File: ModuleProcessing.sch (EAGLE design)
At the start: 24 parts, among them IC1 INA128U, IC2 LM358MX, IC3 MCP606-I_SN

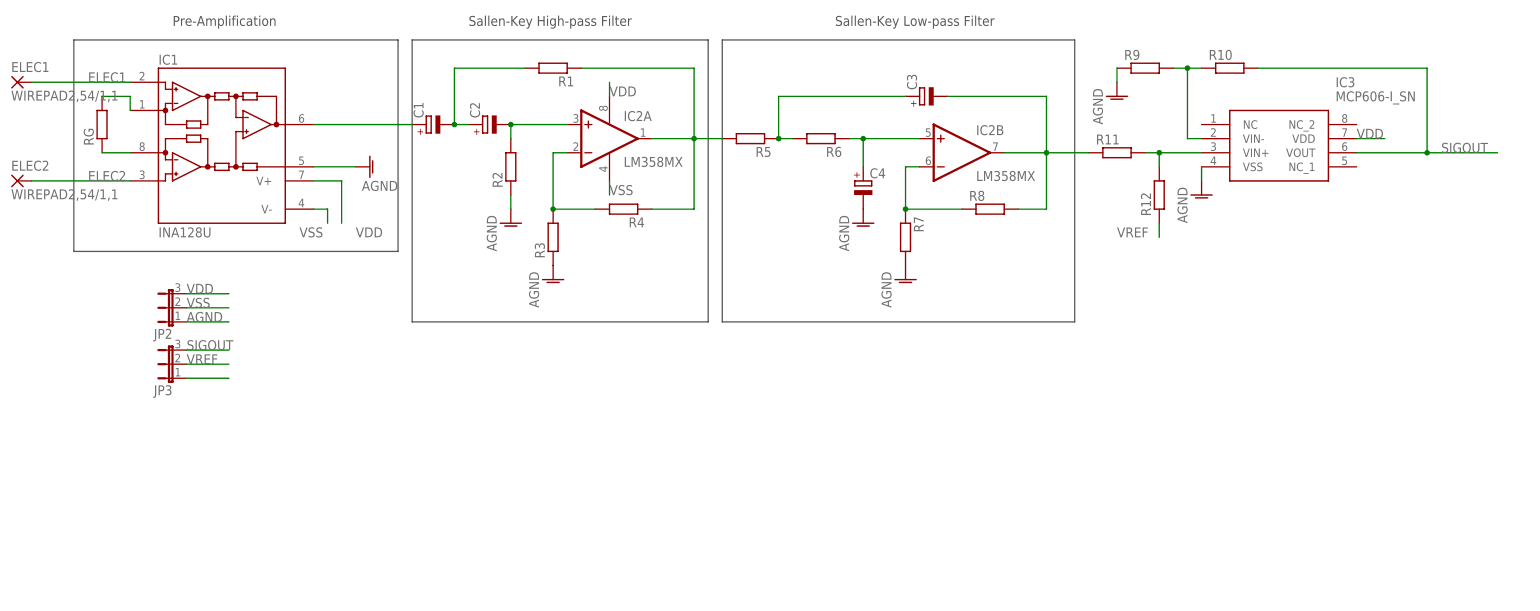
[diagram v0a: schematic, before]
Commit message: Added bypass capacitors on Processing Module
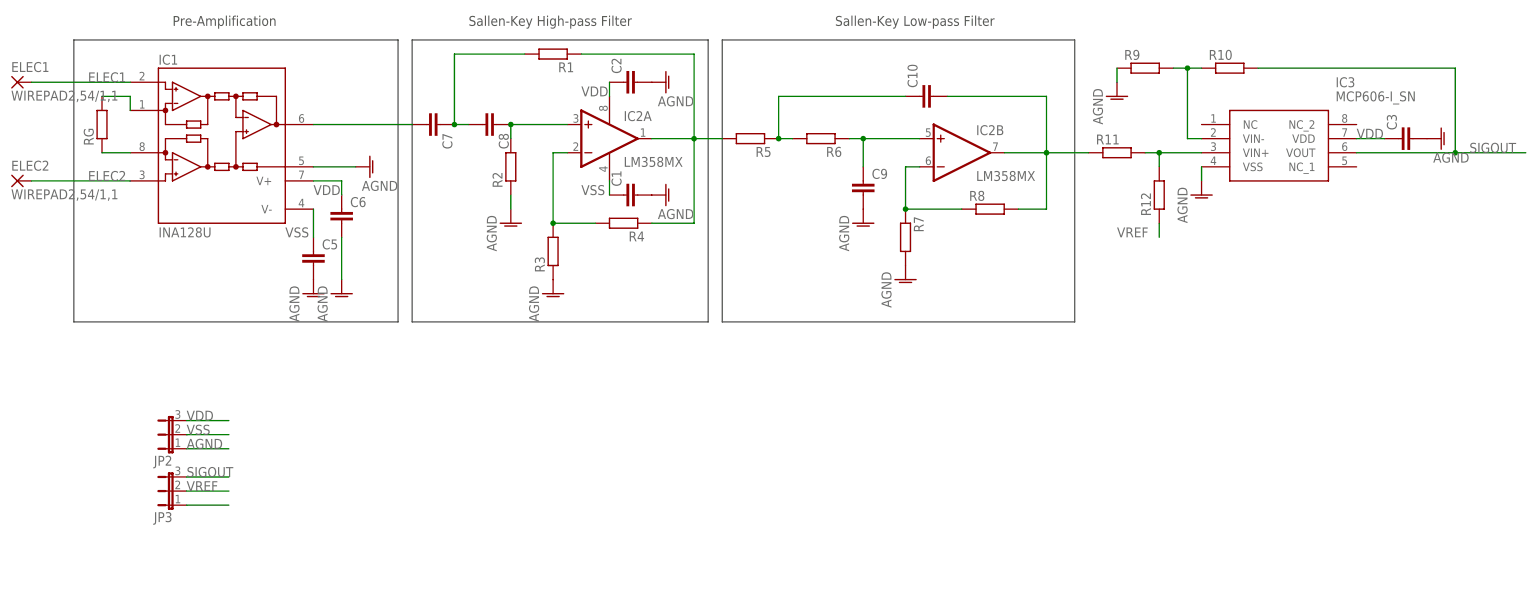
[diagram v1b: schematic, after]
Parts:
- removed C4: (no value), rcl:CPOL-EUE3.5-8
- added C10, C5, C6, C7, C8, C9: (no value), rcl:C-EUC0603
- C1, C2, C3: device rcl:CPOL-EUE3.5-8 -> rcl:C-EUC0603
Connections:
- net AGND: now also C1.2, C2.2, C3.2, C5.2, C6.2, C9.2; no longer C4.-
- net N$10: now also C10.2; no longer C3.-
- net N$5: now also C8.1; no longer C2.-
- net N$6: now also C7.1, C8.2; no longer C1.-, C2.+
- net N$7: now also C7.2; no longer C1.+
- net N$8: now also C10.1; no longer C3.+
- net N$9: now also C9.1; no longer C4.+
- net VDD: now also C2.1, C3.1, C6.1
- net VSS: now also C1.1, C5.1
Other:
- moved on the sheet: JP2, JP3, R1, R3, R4

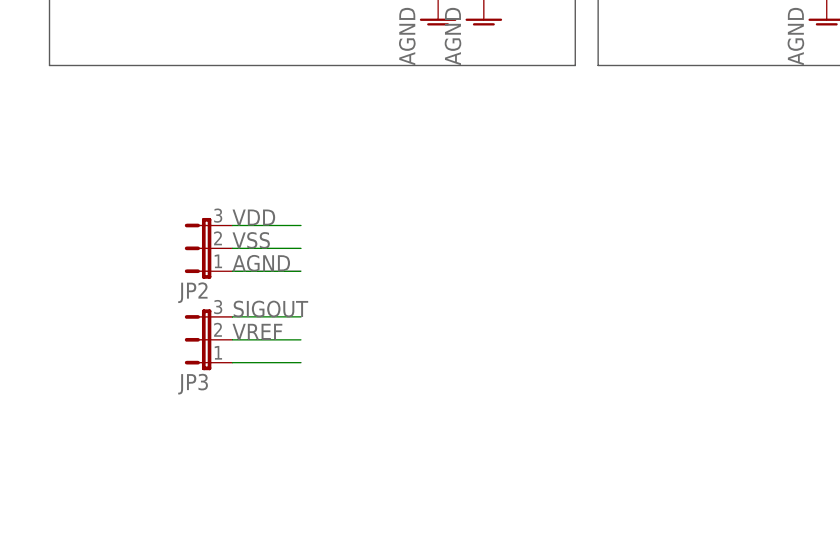
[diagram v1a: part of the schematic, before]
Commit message: Changed board for testing before final prototype
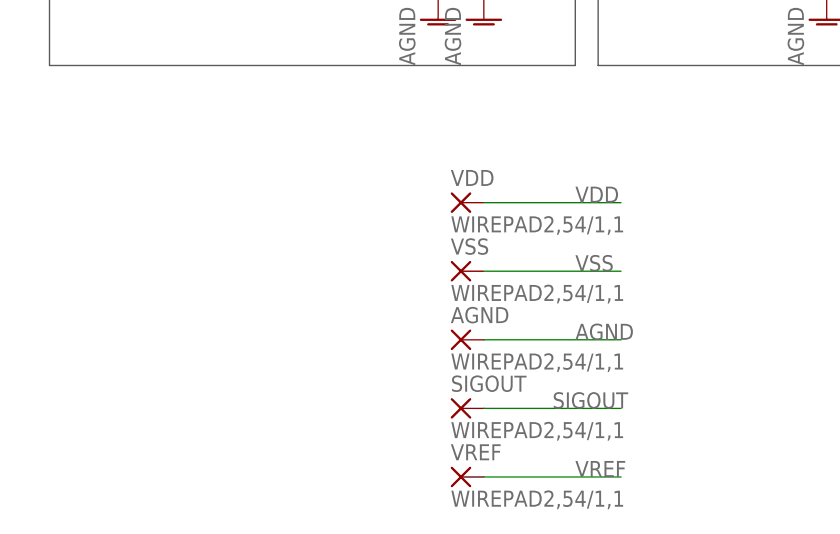
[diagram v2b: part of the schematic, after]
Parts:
- removed JP2, JP3: (no value), jumper:JP2E
- added AGND, SIGOUT, VDD, VREF, VSS: WIREPAD2,54/1,1, wirepad:WIREPAD2,54/1,1
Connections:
- removed net N$19: JP3.1
- net AGND: now also AGND.P; no longer JP2.1
- net SIGOUT: now also SIGOUT.P; no longer JP3.3
- net VDD: now also VDD.P; no longer JP2.3
- net VREF: now also VREF.P; no longer JP3.2
- net VSS: now also VSS.P; no longer JP2.2
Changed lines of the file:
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@@
 </variantdefs>
 <classes>
-<class number="0" name="default" width="0.254" drill="0.3048">
+<class number="0" name="default" width="0.4064" drill="0.5588">
 <clearance class="0" value="0.254"/>
 </class>
@@
 <part name="ELEC1" library="wirepad" library_urn="urn:adsk.eagle:library:412" deviceset="WIREPAD" device="2,54/1,1" package3d_urn="urn:adsk.eagle:package:30836/1"/>
 <part name="ELEC2" library="wirepad" library_urn="urn:adsk.eagle:library:412" deviceset="WIREPAD" device="2,54/1,1" package3d_urn="urn:adsk.eagle:package:30836/1"/>
-<part name="JP2" library="jumper" library_urn="urn:adsk.eagle:library:252" deviceset="JP2E" device="" package3d_urn="urn:adsk.eagle:package:15452/1"/>
-<part name="JP3" library="jumper" library_urn="urn:adsk.eagle:library:252" deviceset="JP2E" device="" package3d_urn="urn:adsk.eagle:package:15452/1"/>
 <part name="C5" library="rcl" library_urn="urn:adsk.eagle:library:334" deviceset="C-EU" device="C0603" package3d_urn="urn:adsk.eagle:package:23616/2"/>
 <part name="C6" library="rcl" library_urn="urn:adsk.eagle:library:334" deviceset="C-EU" device="C0603" package3d_urn="urn:adsk.eagle:package:23616/2"/>
@@
 <part name="C3" library="rcl" library_urn="urn:adsk.eagle:library:334" deviceset="C-EU" device="C0603" package3d_urn="urn:adsk.eagle:package:23616/2"/>
 <part name="AGND12" library="supply1" library_urn="urn:adsk.eagle:library:371" deviceset="AGND" device=""/>
+<part name="VDD" library="wirepad" library_urn="urn:adsk.eagle:library:412" deviceset="WIREPAD" device="2,54/1,1" package3d_urn="urn:adsk.eagle:package:30836/1"/>
+<part name="VSS" library="wirepad" library_urn="urn:adsk.eagle:library:412" deviceset="WIREPAD" device="2,54/1,1" package3d_urn="urn:adsk.eagle:package:30836/1"/>
+<part name="AGND" library="wirepad" library_urn="urn:adsk.eagle:library:412" deviceset="WIREPAD" device="2,54/1,1" package3d_urn="urn:adsk.eagle:package:30836/1"/>
+<part name="SIGOUT" library="wirepad" library_urn="urn:adsk.eagle:library:412" deviceset="WIREPAD" device="2,54/1,1" package3d_urn="urn:adsk.eagle:package:30836/1"/>
+<part name="VREF" library="wirepad" library_urn="urn:adsk.eagle:library:412" deviceset="WIREPAD" device="2,54/1,1" package3d_urn="urn:adsk.eagle:package:30836/1"/>
 </parts>
 <sheets>
@@
 <instance part="ELEC1" gate="G$1" x="12.7" y="66.04"/>
 <instance part="ELEC2" gate="G$1" x="12.7" y="48.26"/>
-<instance part="JP2" gate="1" x="40.64" y="2.54" rot="R90"/>
-<instance part="JP3" gate="1" x="40.64" y="-7.62" rot="R90"/>
 <instance part="C5" gate="G$1" x="66.04" y="35.56"/>
 <instance part="C6" gate="G$1" x="71.12" y="43.18"/>
@@
 <instance part="C3" gate="G$1" x="261.62" y="55.88" rot="R90"/>
 <instance part="AGND12" gate="VR1" x="269.24" y="55.88" rot="R90"/>
+<instance part="VDD" gate="G$1" x="68.58" y="7.62"/>
+<instance part="VSS" gate="G$1" x="68.58" y="0"/>
+<instance part="AGND" gate="G$1" x="68.58" y="-7.62"/>
+<instance part="SIGOUT" gate="G$1" x="68.58" y="-15.24"/>
+<instance part="VREF" gate="G$1" x="68.58" y="-22.86"/>
 </instances>
 <busses>
@@
 </segment>
 <segment>
-<pinref part="JP2" gate="1" pin="1"/>
-<wire x1="43.18" y1="0" x2="50.8" y2="0" width="0.1524" layer="91"/>
-<label x="43.18" y="0" size="1.778" layer="95"/>
-</segment>
-<segment>
 <pinref part="C5" gate="G$1" pin="2"/>
 <pinref part="AGND8" gate="VR1" pin="AGND"/>
@@
 <pinref part="C3" gate="G$1" pin="2"/>
 <pinref part="AGND12" gate="VR1" pin="AGND"/>
+</segment>
+<segment>
+<pinref part="AGND" gate="G$1" pin="P"/>
+<wire x1="71.12" y1="-7.62" x2="86.36" y2="-7.62" width="0.1524" layer="91"/>
+<label x="81.28" y="-7.62" size="1.778" layer="95"/>
 </segment>
 </net>
@@
 </segment>
 <segment>
-<pinref part="JP3" gate="1" pin="3"/>
-<wire x1="43.18" y1="-5.08" x2="50.8" y2="-5.08" width="0.1524" layer="91"/>
-<label x="43.18" y="-5.08" size="1.778" layer="95"/>
+<pinref part="SIGOUT" gate="G$1" pin="P"/>
+<wire x1="71.12" y1="-15.24" x2="86.36" y2="-15.24" width="0.1524" layer="91"/>
+<label x="78.74" y="-15.24" size="1.778" layer="95"/>
 </segment>
 </net>
@@
 <label x="114.3" y="63.5" size="1.778" layer="95"/>
 <pinref part="C2" gate="G$1" pin="1"/>
-</segment>
-<segment>
-<pinref part="JP2" gate="1" pin="3"/>
-<wire x1="43.18" y1="5.08" x2="50.8" y2="5.08" width="0.1524" layer="91"/>
-<label x="43.18" y="5.08" size="1.778" layer="95"/>
 </segment>
 <segment>
@@
 <label x="66.04" y="45.72" size="1.778" layer="95"/>
 </segment>
+<segment>
+<pinref part="VDD" gate="G$1" pin="P"/>
+<wire x1="71.12" y1="7.62" x2="86.36" y2="7.62" width="0.1524" layer="91"/>
+<label x="81.28" y="7.62" size="1.778" layer="95"/>
+</segment>
 </net>
 <net name="VSS" class="0">
@@
 </segment>
 <segment>
-<pinref part="JP2" gate="1" pin="2"/>
-<wire x1="43.18" y1="2.54" x2="50.8" y2="2.54" width="0.1524" layer="91"/>
-<label x="43.18" y="2.54" size="1.778" layer="95"/>
-</segment>
-<segment>
 <pinref part="IC1" gate="G$1" pin="V-"/>
 <pinref part="C5" gate="G$1" pin="1"/>
@@
 <label x="60.96" y="38.1" size="1.778" layer="95"/>
 </segment>
+<segment>
+<pinref part="VSS" gate="G$1" pin="P"/>
+<wire x1="71.12" y1="0" x2="86.36" y2="0" width="0.1524" layer="91"/>
+<label x="81.28" y="0" size="1.778" layer="95"/>
+</segment>
 </net>
 <net name="VREF" class="0">
-<segment>
-<pinref part="JP3" gate="1" pin="2"/>
-<wire x1="43.18" y1="-7.62" x2="50.8" y2="-7.62" width="0.1524" layer="91"/>
-<label x="43.18" y="-7.62" size="1.778" layer="95"/>
-</segment>
 <segment>
 <pinref part="R12" gate="G$1" pin="1"/>
@@
 <label x="210.82" y="38.1" size="1.778" layer="95"/>
 </segment>
-</net>
-<net name="N$19" class="0">
-<segment>
-<pinref part="JP3" gate="1" pin="1"/>
-<wire x1="43.18" y1="-10.16" x2="50.8" y2="-10.16" width="0.1524" layer="91"/>
-</segment>
-</net>
+<segment>
+<pinref part="VREF" gate="G$1" pin="P"/>
+<wire x1="71.12" y1="-22.86" x2="86.36" y2="-22.86" width="0.1524" layer="91"/>
+<label x="81.28" y="-22.86" size="1.778" layer="95"/>
+</segment>
+</net>

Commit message: Final version of processing pre-prototype
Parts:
- removed C10: (no value), rcl:C-EUC0603
- removed R1: (no value), rcl:R-EU_0207/10
- added C4: (no value), rcl:C-EUC0603
- added R13: (no value), rcl:R-EU_0207/10
- renumbered AGND to PAD5, ELEC1 to PAD1, ELEC2 to PAD2, SIGOUT to PAD6, VDD to PAD3, VREF to PAD7, VSS to PAD4
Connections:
- net AGND: now also C7.2, R11.1, R4.1, R8.2; no longer C3.2, R3.1, R7.2, R9.1
- net N$10: now also C8.2, R10.1, R9.2; no longer C10.2, R11.1, R8.2
- net N$11: now also R9.1; no longer R7.1
- net N$12: now also R10.2; no longer R11.2
- net N$13: now also R11.2, R13.1; no longer R10.1, R9.2
- net N$3: now also R5.2; no longer R3.2
- net N$4: now also R3.1, R5.1, R6.2; no longer R1.1, R4.1, R5.2
- net N$5: now also C4.1; no longer C8.1
- net N$6: now also C3.1, C4.2, R3.2; no longer C7.1, C8.2, R1.2
- net N$7: now also C3.2; no longer C7.2
- net N$8: now also C8.1, R6.1, R7.2; no longer C10.1, R5.1, R6.2
- net N$9: now also C7.1, R7.1; no longer C9.1, R6.1
- net SIGOUT: now also R13.2; no longer R10.2
- net VDD: now also C5.1, C9.1; no longer C3.1, C6.1
- net VSS: now also C6.1; no longer C5.1
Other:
- moved on the sheet: C1, C2, C3, C5, C6, C7, C8, C9, R10, R11, R3, R4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
